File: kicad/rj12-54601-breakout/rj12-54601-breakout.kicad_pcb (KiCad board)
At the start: 2 copper layers, 20.3 x 17.8 mm, 5 parts, among them J1 Conn_01x03, J2 Conn_01x03, SW1 SW_Push, SW2 SW_Push, U1 RJ12

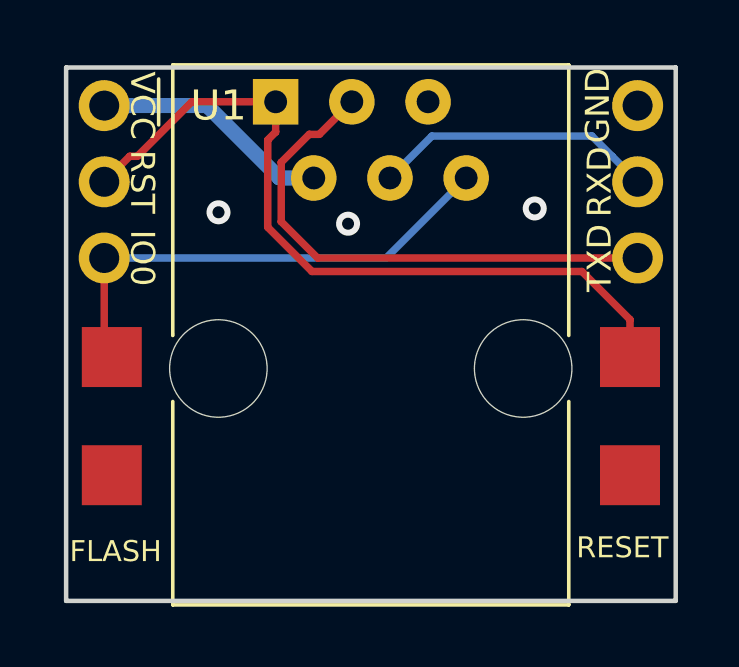
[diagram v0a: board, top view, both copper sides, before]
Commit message: add USB add-on add-on board support
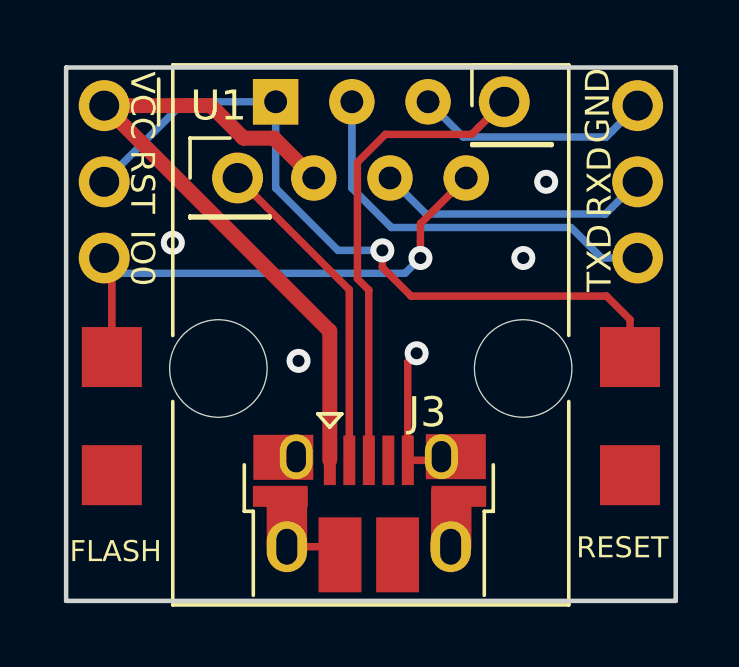
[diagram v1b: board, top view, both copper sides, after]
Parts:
- added J3: USB_B_Micro, Connector_USB:USB_Micro-B_Amphenol_10103594-0001LF_Horizontal, F.Cu at (148.5, 105.0)
- added J4: Conn_01x01_Female, Connector_PinHeader_2.54mm:PinHeader_1x01_P2.54mm_Vertical, F.Cu at (153.3, 91.4)
- added J5: Conn_01x01_Female, Connector_PinHeader_2.54mm:PinHeader_1x01_P2.54mm_Vertical, F.Cu at (143.9, 93.9)
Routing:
- net /D+: track 0.00 -> 15.8 mm
- net GND: track 0.00 -> 15.1 mm, vias 3 -> 5
- net VCC: track 7.98 -> 22.9 mm
- net /D-: track 0.00 -> 11.0 mm
- net /TXD: track 17.5 -> 13.4 mm
- net /IO0: track 16.6 -> 17.7 mm, vias 0 -> 1
- net /RESET: track 25.7 -> 24.9 mm, vias 0 -> 1
